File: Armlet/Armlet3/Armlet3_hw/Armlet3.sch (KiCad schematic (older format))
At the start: 146 parts, among them M1 MOTOR, Q1 MMBT2222, Q2 MMBT2222, Q3 TSOP75256, Q4 IRLML6302, Q5 BC848CL, Q6 MMBT2222, SW1 BUTTON, SW2 BUTTON, SW3 BUTTON, SW4 BUTTON, SW5 BUTTON, SW6 BUTTON, SW7 BUTTON, SW8 BUTTON, SW9 BUTTON

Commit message: 
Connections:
- net labels added: LCD_DA0_SDA, LCD_DA1, LCD_DA2, LCD_DA3, LCD_DA4, LCD_DA5, LCD_DA6, LCD_DA7, LCD_DC_SCLK, LCD_PAR_SPI, LCD_RD, LCD_WR
- net labels removed: LCD_SCLK, LCD_SDA
- wire segments 476 -> 484
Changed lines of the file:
@@
-EESchema Schematic File Version 2  date 2/26/2013 5:42:32 PM
+EESchema Schematic File Version 2  date 2/26/2013 7:36:17 PM
 LIBS:Connectors_kl
 LIBS:display_kl
@@
 $EndDescr
 Wire Wire Line
-	9200 8450 9700 8450
+	12950 9950 13150 9950
+Wire Wire Line
+	12950 9750 13150 9750
+Wire Wire Line
+	9050 7850 9700 7850
+Wire Wire Line
+	12950 9350 13150 9350
+Wire Wire Line
+	12950 9050 13150 9050
+Wire Wire Line
+	9700 7750 9050 7750
+Wire Wire Line
+	9700 7550 9050 7550
+Wire Wire Line
+	9700 7350 9050 7350
+Wire Wire Line
+	9700 7150 9050 7150
+Wire Wire Line
+	1850 1300 1950 1300
+Wire Wire Line
+	1850 1500 1950 1500
+Wire Wire Line
+	1850 1700 1950 1700
+Wire Wire Line
+	1850 1900 1950 1900
+Wire Wire Line
+	1850 2300 1950 2300
+Wire Wire Line
+	13350 10450 13850 10450
 Wire Wire Line
 	13700 6850 13700 5350
@@
 Wire Wire Line
 	13150 6250 12950 6250
-Wire Wire Line
-	9400 7850 9700 7850
-Wire Wire Line
-	9400 7650 9700 7650
-Wire Wire Line
-	9400 7350 9700 7350
 Connection ~ 7450 9850
 Wire Wire Line
@@
 	13850 12050 13850 11250
 Wire Wire Line
-	9300 8250 9700 8250
+	14150 10400 14550 10400
 Wire Wire Line
-	9300 8050 9700 8050
-Wire Wire Line
-	9700 7150 9400 7150
+	14150 10200 14550 10200
 Wire Wire Line
 	16350 11750 16250 11750
@@
 	21500 12000 21500 11800
 Wire Wire Line
-	9300 7550 9700 7550
+	9300 7950 9700 7950
 Connection ~ 13000 14550
 Wire Wire Line
@@
 Connection ~ 2650 3200
 Wire Wire Line
-	1850 1700 2000 1700
-Connection ~ 1900 2100
-Wire Wire Line
-	1900 2600 1900 1300
-Wire Wire Line
-	1900 2600 1850 2600
-Connection ~ 1900 1600
-Wire Wire Line
-	1900 1600 1850 1600
-Connection ~ 1900 1900
-Wire Wire Line
-	1900 1900 1850 1900
-Connection ~ 1900 1500
-Wire Wire Line
-	1900 1500 1850 1500
-Wire Wire Line
 	20650 2650 20650 2400
 Wire Wire Line
@@
 Connection ~ 20650 2650
 Wire Wire Line
-	1900 1300 1850 1300
-Wire Wire Line
-	1900 2100 1850 2100
-Connection ~ 1900 1700
-Wire Wire Line
-	1900 1800 1850 1800
-Connection ~ 1900 1800
-Wire Wire Line
-	1850 1400 1900 1400
-Connection ~ 1900 1400
-Wire Wire Line
-	1900 2300 1850 2300
-Connection ~ 1900 2300
-Wire Wire Line
 	2650 3350 2650 3200
 Wire Wire Line
@@
 	16250 11400 16350 11400
 Wire Wire Line
-	9400 7250 9700 7250
-Wire Wire Line
-	9400 7050 9700 7050
-Wire Wire Line
-	9700 8150 9300 8150
+	14550 10300 14150 10300
 Wire Wire Line
-	9700 8350 9300 8350
+	14550 10500 14150 10500
 Wire Wire Line
 	21500 7500 21500 7450
@@
 	12950 9150 13050 9150
 Wire Wire Line
-	9700 7450 9400 7450
+	12950 7050 13050 7050
 Wire Wire Line
-	9700 7750 9400 7750
+	13050 7750 12950 7750
 Wire Wire Line
-	9700 7950 9400 7950
+	1950 2600 1850 2600
 Wire Wire Line
-	12950 7050 13050 7050
+	1950 2100 1850 2100
 Wire Wire Line
-	13050 7750 12950 7750
-Text Label 9200 8450 0    60   ~ 0
+	1950 1800 1850 1800
+Wire Wire Line
+	1950 1600 1850 1600
+Wire Wire Line
+	1950 1400 1850 1400
+Wire Wire Line
+	9050 7050 9700 7050
+Wire Wire Line
+	9050 7250 9700 7250
+Wire Wire Line
+	9050 7450 9700 7450
+Wire Wire Line
+	9050 7650 9700 7650
+Wire Wire Line
+	13150 8950 12950 8950
+Wire Wire Line
+	13150 9250 12950 9250
+Wire Wire Line
+	13150 9550 12950 9550
+Wire Wire Line
+	13150 9650 12950 9650
+Wire Wire Line
+	13150 9850 12950 9850
+Text Label 6200 8100 0    60   ~ 0
+LCD_DC_SCLK
+Text Label 6200 8000 0    60   ~ 0
+LCD_RD
+Text Label 9050 7850 0    60   ~ 0
+LCD_WR
+Text Label 6200 8600 0    60   ~ 0
+LCD_PAR_SPI
+Text Label 9100 5850 0    60   ~ 0
+LCD_DA0_SDA
+Text Label 9100 5650 0    60   ~ 0
+LCD_DC_SCLK
+Text Label 15800 9700 0    60   ~ 0
+LCD_XRES
+Text Label 15800 9900 0    60   ~ 0
+LCD_XCS
+Text Label 9050 7050 0    60   ~ 0
+LCD_DA0_SDA
+Text Label 15800 9400 0    60   ~ 0
+LCD_DC_SCLK
+Text Label 9050 7150 0    60   ~ 0
+LCD_DA1
+Text Label 9050 7250 0    60   ~ 0
+LCD_DA2
+Text Label 9050 7350 0    60   ~ 0
+LCD_DA3
+Text Label 9050 7450 0    60   ~ 0
+LCD_DA4
+Text Label 9050 7550 0    60   ~ 0
+LCD_DA5
+Text Label 9050 7650 0    60   ~ 0
+LCD_DA6
+Text Label 9050 7750 0    60   ~ 0
+LCD_DA7
+Text Label 15800 9300 0    60   ~ 0
+LCD_RD
+Text Label 15800 9500 0    60   ~ 0
+LCD_WR
+Text Label 15800 9800 0    60   ~ 0
+LCD_PAR_SPI
+Text Label 1950 2600 0    60   ~ 0
+LCD_PAR_SPI
+Text Label 1950 2300 0    60   ~ 0
+LCD_WR
+Text Label 1950 2100 0    60   ~ 0
+LCD_RD
+Text Label 1950 1900 0    60   ~ 0
+LCD_DA7
+Text Label 1950 1800 0    60   ~ 0
+LCD_DA6
+Text Label 1950 1700 0    60   ~ 0
+LCD_DA5
+Text Label 1950 1600 0    60   ~ 0
+LCD_DA4
+Text Label 1950 1500 0    60   ~ 0
+LCD_DA3
+Text Label 1950 1400 0    60   ~ 0
+LCD_DA2
+Text Label 1950 1300 0    60   ~ 0
+LCD_DA1
+$Comp
+L STM32F205VX-100 DD?
+U 1 1 512C8AE1
+P 11350 7750
+F 0 "DD?" H 10750 10350 60  0000 C CNN
+F 1 "STM32F205VX-100" H 11400 10350 60  0000 C CNN
+	1    11350 7750
+	1    0    0    -1
+$EndComp
+Text Label 13350 10450 0    60   ~ 0
 PeriphPwr
 Text Label 14250 3100 0    60   ~ 0
@@
 $EndComp
 $Comp
-L STM32F205VX-100 DD?
-U 1 1 512C8AE1
-P 11350 7750
-F 0 "DD?" H 10750 10350 60  0000 C CNN
-F 1 "STM32F205VX-100" H 11400 10350 60  0000 C CNN
-	1    11350 7750
-	1    0    0    -1
-$EndComp
-$Comp
 L GND #PWR?
 U 1 1 50D78699
@@
 	1    0    0    -1
 $EndComp
-Text Label 9400 7750 0    60   ~ 0
+Text Label 13150 9750 0    60   ~ 0
 Btn7
-Text Label 9400 7850 0    60   ~ 0
+Text Label 13150 9850 0    60   ~ 0
 Btn8
-Text Label 9400 7950 0    60   ~ 0
+Text Label 13150 9950 0    60   ~ 0
 Btn9
-Text Label 9400 7350 0    60   ~ 0
+Text Label 13150 9350 0    60   ~ 0
 Btn4
-Text Label 9400 7450 0    60   ~ 0
+Text Label 13150 9550 0    60   ~ 0
 Btn5
-Text Label 9400 7650 0    60   ~ 0
+Text Label 13150 9650 0    60   ~ 0
 Btn6
-Text Label 9400 7050 0    60   ~ 0
+Text Label 13150 8950 0    60   ~ 0
 Btn1
-Text Label 9400 7150 0    60   ~ 0
+Text Label 13150 9050 0    60   ~ 0
 Btn2
-Text Label 9400 7250 0    60   ~ 0
+Text Label 13150 9250 0    60   ~ 0
 Btn3
 Text Label 16350 12100 0    60   ~ 0
@@
 	1    0    0    -1
 $EndComp
-Text Label 9300 8250 0    60   ~ 0
+Text Label 14150 10400 0    60   ~ 0
 P2_SDA
-Text Label 9300 8350 0    60   ~ 0
+Text Label 14150 10500 0    60   ~ 0
 P2_SCL
-Text Label 9300 8050 0    60   ~ 0
+Text Label 14150 10200 0    60   ~ 0
 P1_SCL
-Text Label 9300 8150 0    60   ~ 0
+Text Label 14150 10300 0    60   ~ 0
 P1_SDA
 Text Notes 3250 5750 0    60   ~ 0
@@
 $EndComp
 $Comp
-L GND #PWR057
-U 1 1 5093C9A8
-P 2000 1700
-F 0 "#PWR057" H 2090 1680 30  0001 C CNN
-F 1 "GND" H 2000 1620 30  0001 C CNN
-	1    2000 1700
-	0    -1   -1   0
-$EndComp
-$Comp
 L +3.3V #PWR058
 U 1 1 5093C9EA
@@
 Text Label 6350 2400 0    60   ~ 0
 CC_GDO2
-Text Label 9300 7550 0    60   ~ 0
+Text Label 9300 7950 0    60   ~ 0
 Vibro
 $Comp
@@
 Text Label 9100 5550 0    60   ~ 0
 LCD_XCS
-Text Label 9100 5850 0    60   ~ 0
-LCD_SDA
-Text Label 9100 5650 0    60   ~ 0
-LCD_SCLK
 Text Label 9100 6150 0    60   ~ 0
 LCD_BCKLT
@@
 LCD_BCKLT
 Text Label 1950 2200 0    60   ~ 0
-LCD_SCLK
+LCD_DC_SCLK
 Text Label 1950 1200 0    60   ~ 0
-LCD_SDA
+LCD_DA0_SDA
 Text Label 1950 2700 0    60   ~ 0
 LCD_XCS

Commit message: Armlet3 PCB started
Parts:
- removed ANT1: ANT_PCB_MONO_GND, symbol ANT_PCB_MONO_GND
- removed R42, R43: 4K7, RES_0402, symbol R
- removed R44: 150, RES_0603, symbol R
- removed XL5: CONN_2, symbol CONN_2
- added ANT1: ANT_PCB_MONO, symbol ANT_PCB_MONO
- added C48: 1u, symbol C
- added DA5: NCP583SQ, symbol NCP583SQ
- added Q7: BC848CL, symbol NPN
- added R15: 1k, RES_0402, symbol R
- added R16, R17: 10k, RES_0402, symbol R
- added XL5: CONN_3, symbol CONN_3
- Q4: value IRLML6302 -> IRLML9303
- gave numbers to parts that had none: 10
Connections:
- net labels added: LCD_DA0, LCD_DC, P_SCL, P_SDA, RX2
- net labels removed: LCD_DA0_SDA, LCD_DC_SCLK, LCD_PAR_SPI, P1_SCL, P1_SDA, P2_SCL, P2_SDA, PeriphPwr2
- wire segments 484 -> 492
- no-connect marks 9 -> 19
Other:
- note added: "DEBUG \nTX/RX"
- note added: "Peripherals usage\n\nSDIO - SD Card\nUSB\n\nUART2 - debug output\nUART4 - klNFC\n\nSPI1 - CC (Radio) Bus\nSPI2 - Audio Bus\nSPI3 - LCD data link\n\nTIM1 Ch4 - Vibro\nTIM2 Ch3 - klNFC TX\nTIM2 ETR - klNFC modulation in\nTIM3 Ch2 - Xotar LED\nTIM4 Ch1 - Buzzer\nTIM5 - Xotar Data timings\nTIM8 Ch1 - Xotar In\nTIM10 Ch1 - LCD backlight\n\nEXTI0 - VS data request\nEXTI1 - klNFC IRQ\nEXTI2 - Acc IRQ (?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"
- note added: "Pill \nConnectors"
- note removed: "DEBUG \nOutput"
- note removed: "Double Periph Connector"
- note removed: "Peripheral Power"
- note removed: "Peripherals usage\n\nSDIO - SD Card\nUSB\n\nUART2 - debug output\nUART4 - klNFC\n\nSPI1 - CC (Radio) Bus\nSPI2 - Audio Bus\nSPI3 - LCD data link\n\nTIM2 Ch3 - klNFC TX\nTIM2 ETR - klNFC modulation in\nTIM3 Ch2 - Xotar LED\nTIM4 Ch1 - Buzzer\nTIM5 - Xotar Data timings\nTIM8 Ch1 - Xotar In\nTIM9 Ch1 - Vibro\nTIM10 Ch1 - LCD backlight\n\nEXTI 0 - VS data request\nEXTI 1 - klNFC IRQ\nEXTI2 - Acc IRQ"
- note removed: "Pill Connector"
- note removed: "Replace VCap1 \nand VCap2 with\n0R resistors in case\nof stm32f10x CPU"
- moved on the sheet: C20, C21, C26, C27, C28, C29, C36, C37, C38, C39, C40, C41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

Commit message: Armlet3 PCB completed
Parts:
- added C62, C63: *, symbol C
- added C64: 1u, symbol C
- added L8: *, IND_0402, symbol L
- added R19: 1k, RES_0402, symbol R
- added XL7: CONN_1, symbol CONN_1
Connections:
- net labels removed: I2C_PullPwr
- wire segments 492 -> 500
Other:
- note added: "Debug\nconnector"
- note added: "Matching circuit"
- moved on the sheet: ANT1

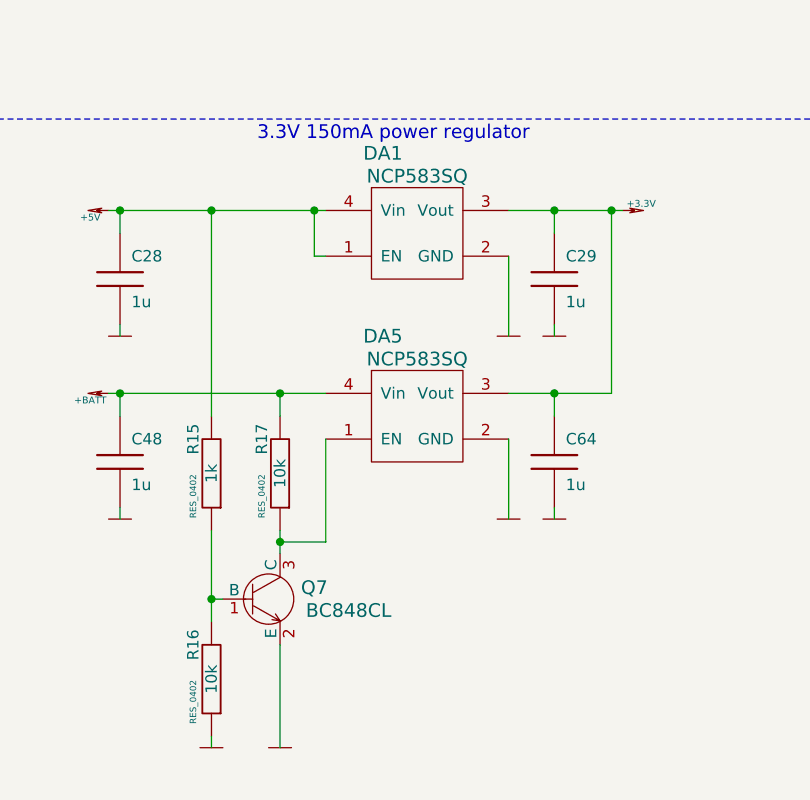
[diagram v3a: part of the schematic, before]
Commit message: 
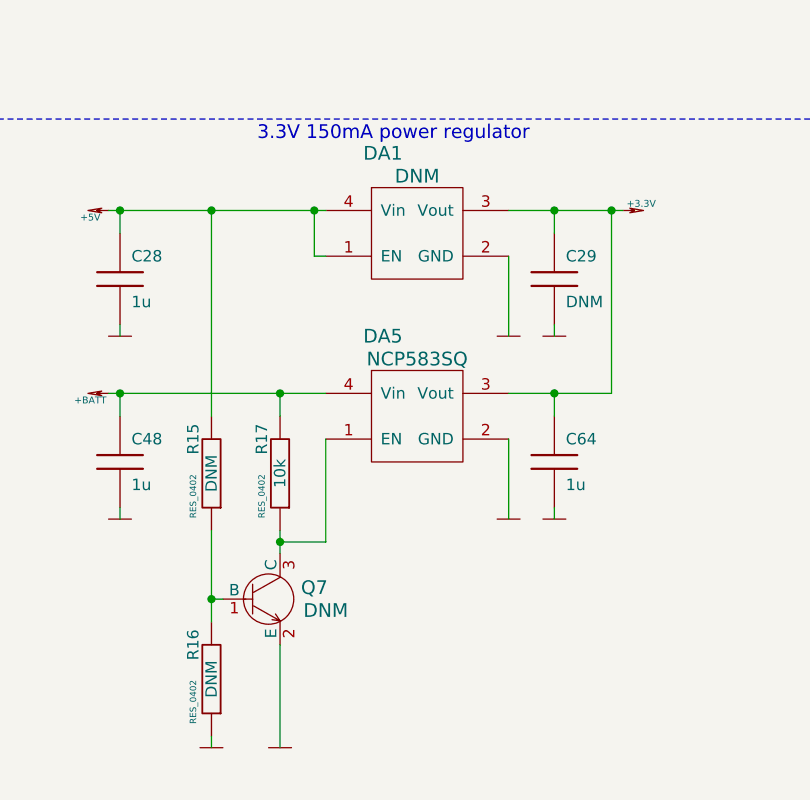
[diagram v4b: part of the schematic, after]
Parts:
- C29: value 1u -> DNM
- DA1: value NCP583SQ -> DNM
- Q7: value BC848CL -> DNM
- R15: value 1k -> DNM
- R16: value 10k -> DNM
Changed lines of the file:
@@
-EESchema Schematic File Version 2  date 09/03/2013 20:02:22
+EESchema Schematic File Version 2  date 21/03/2013 00:28:37
 LIBS:Connectors_kl
 LIBS:display_kl
@@
 Sheet 1 1
 Title ""
-Date "9 mar 2013"
+Date "20 mar 2013"
 Rev ""
 Comp ""
@@
 P 6600 15550
 F 0 "R16" V 6680 15400 50  0000 C CNN
-F 1 "10k" V 6600 15550 50  0000 C CNN
+F 1 "DNM" V 6600 15550 50  0000 C CNN
 F 2 "RES_0402" V 6680 15650 28  0000 C CNN
 F 3 "" H 6600 15550 60  0001 C CNN
@@
 P 6850 15200
 F 0 "Q7" H 7050 15250 60  0000 C CNN
-F 1 "BC848CL" H 7200 15150 60  0000 C CNN
+F 1 "DNM" H 7100 15150 60  0000 C CNN
 F 2 "" H 6850 15200 60  0001 C CNN
 F 3 "" H 6850 15200 60  0001 C CNN
@@
 P 6600 14650
 F 0 "R15" V 6680 14500 50  0000 C CNN
-F 1 "1k" V 6600 14650 50  0000 C CNN
+F 1 "DNM" V 6600 14650 50  0000 C CNN
 F 2 "RES_0402" V 6680 14750 28  0000 C CNN
 F 3 "" H 6600 14650 60  0001 C CNN
@@
 P 7500 13600
 F 0 "DA1" H 7350 13950 60  0000 C CNN
-F 1 "NCP583SQ" H 7500 13850 60  0000 C CNN
+F 1 "DNM" H 7500 13850 60  0000 C CNN
 F 2 "" H 7500 13600 60  0001 C CNN
 F 3 "" H 7500 13600 60  0001 C CNN
@@
 P 8100 13800
 F 0 "C29" H 8150 13900 50  0000 L CNN
-F 1 "1u" H 8150 13700 50  0000 L CNN
+F 1 "DNM" H 8150 13700 50  0000 L CNN
 F 2 "" H 8100 13800 60  0001 C CNN
 F 3 "" H 8100 13800 60  0001 C CNN

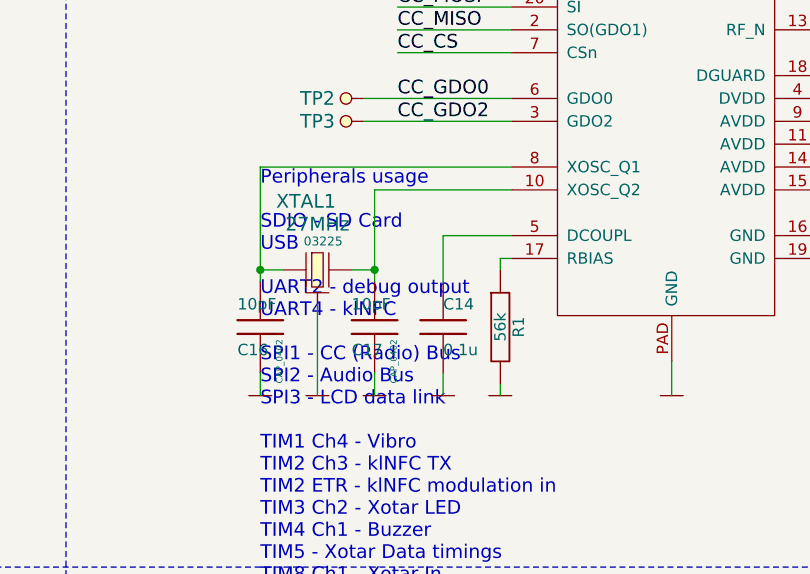
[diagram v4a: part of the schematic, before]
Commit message: 
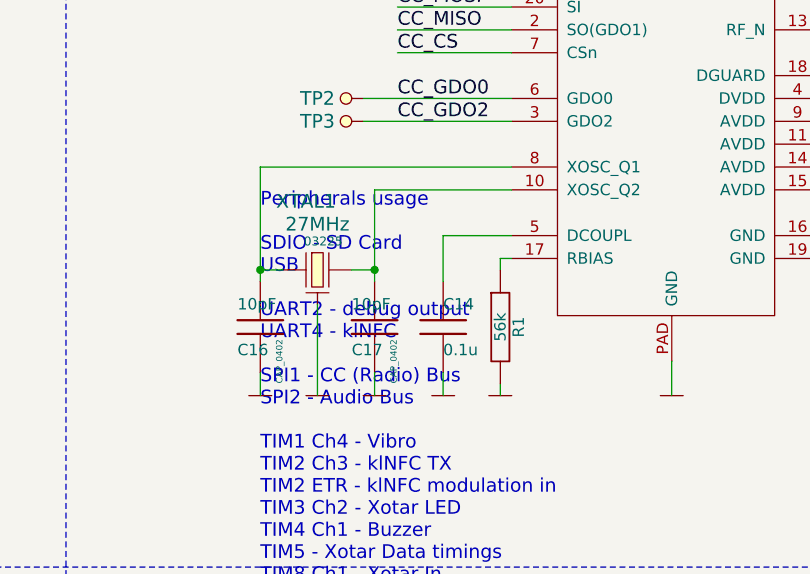
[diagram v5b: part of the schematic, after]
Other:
- note added: "Peripherals usage\n\nSDIO - SD Card\nUSB\n\nUART2 - debug output\nUART4 - klNFC\n\nSPI1 - CC (Radio) Bus\nSPI2 - Audio Bus\n\nTIM1 Ch4 - Vibro\nTIM2 Ch3 - klNFC TX\nTIM2 ETR - klNFC modulation in\nTIM3 Ch2 - Xotar LED\nTIM4 Ch1 - Buzzer\nTIM5 - Xotar Data timings\nTIM8 Ch1 - Xotar In\nTIM10 Ch1 - LCD backlight\n\nEXTI0 - VS data request\nEXTI1 - klNFC IRQ\nEXTI2 - Acc IRQ (?)\nEXTI3 - CC GDO2\nEX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"
- note removed: "Peripherals usage\n\nSDIO - SD Card\nUSB\n\nUART2 - debug output\nUART4 - klNFC\n\nSPI1 - CC (Radio) Bus\nSPI2 - Audio Bus\nSPI3 - LCD data link\n\nTIM1 Ch4 - Vibro\nTIM2 Ch3 - klNFC TX\nTIM2 ETR - klNFC modulation in\nTIM3 Ch2 - Xotar LED\nTIM4 Ch1 - Buzzer\nTIM5 - Xotar Data timings\nTIM8 Ch1 - Xotar In\nTIM10 Ch1 - LCD backlight\n\nEXTI0 - VS data request\nEXTI1 - klNFC IRQ\nEXTI2 - Acc IRQ (?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"

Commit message: Pcb repaired. BOM modified. Radio works.
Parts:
- C26, C27: value 4.7u -> 10u
- C62: value * -> 3.3pF
- C63: value * -> 6.8pF
- C7, C9: value 0.01u -> 10n
- L8: value * -> 15nH
- R7, R9: value 390k -> 330k

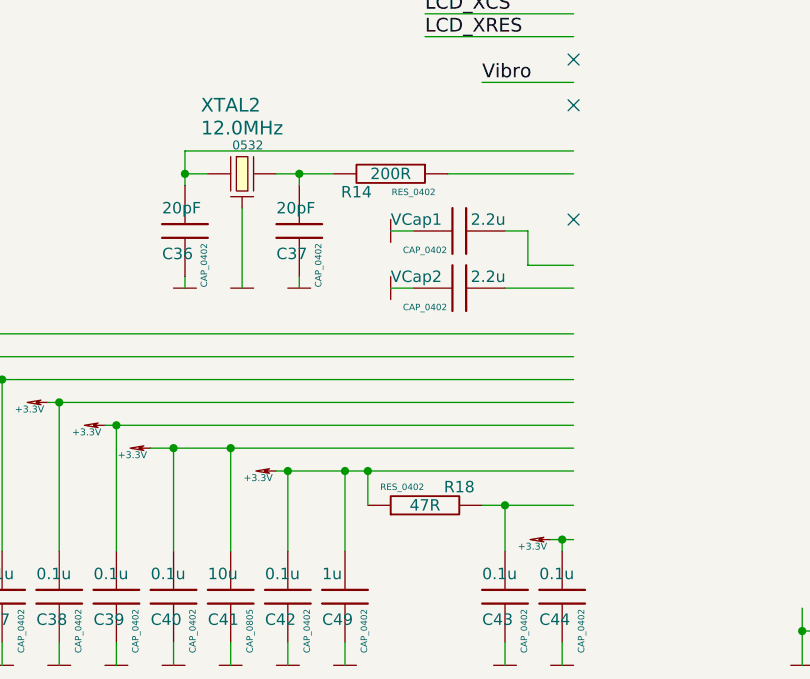
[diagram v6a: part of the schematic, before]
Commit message: Concentrator TX-RX by timeout, low precision due to int ms
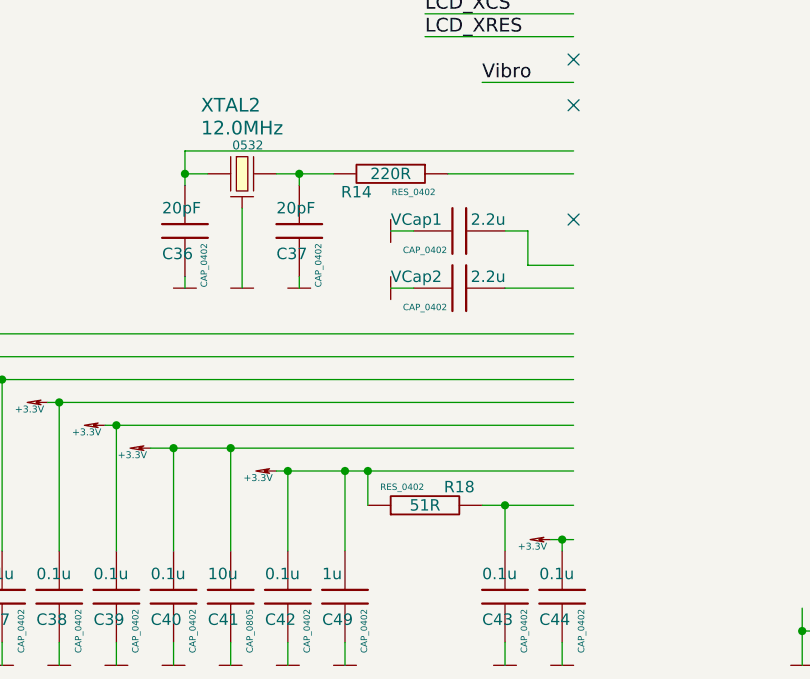
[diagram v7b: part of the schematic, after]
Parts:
- R14: value 200R -> 220R
- R18: value 47R -> 51R
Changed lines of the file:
@@
-EESchema Schematic File Version 2  date 24/03/2013 22:37:34
+EESchema Schematic File Version 2  date 28/03/2013 20:32:23
 LIBS:Connectors_kl
 LIBS:display_kl
@@
 Sheet 1 1
 Title ""
-Date "24 mar 2013"
+Date "28 mar 2013"
 Rev ""
 Comp ""
@@
 P 7650 10300
 F 0 "R18" V 7730 10150 50  0000 C CNN
-F 1 "47R" V 7650 10300 50  0000 C CNN
+F 1 "51R" V 7650 10300 50  0000 C CNN
 F 2 "RES_0402" V 7730 10400 28  0000 C CNN
 F 3 "" H 7650 10300 60  0001 C CNN
@@
 P 7500 8850
 F 0 "R14" V 7580 8700 50  0000 C CNN
-F 1 "200R" V 7500 8850 50  0000 C CNN
+F 1 "220R" V 7500 8850 50  0000 C CNN
 F 2 "RES_0402" V 7580 8950 28  0000 C CNN
 F 3 "" H 7500 8850 60  0001 C CNN
@@
 Connection ~ 8100 14300
 $Comp
-L +3.3V #PWR?
+L +3.3V #PWR0160
 U 1 1 513B5ACD
 P 14700 1550
-F 0 "#PWR?" H 14700 1510 30  0001 C CNN
+F 0 "#PWR0160" H 14700 1510 30  0001 C CNN
 F 1 "+3.3V" H 14780 1580 30  0000 C CNN
 F 2 "" H 14700 1550 60  0001 C CNN
